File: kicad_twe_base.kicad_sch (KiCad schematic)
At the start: 5 parts

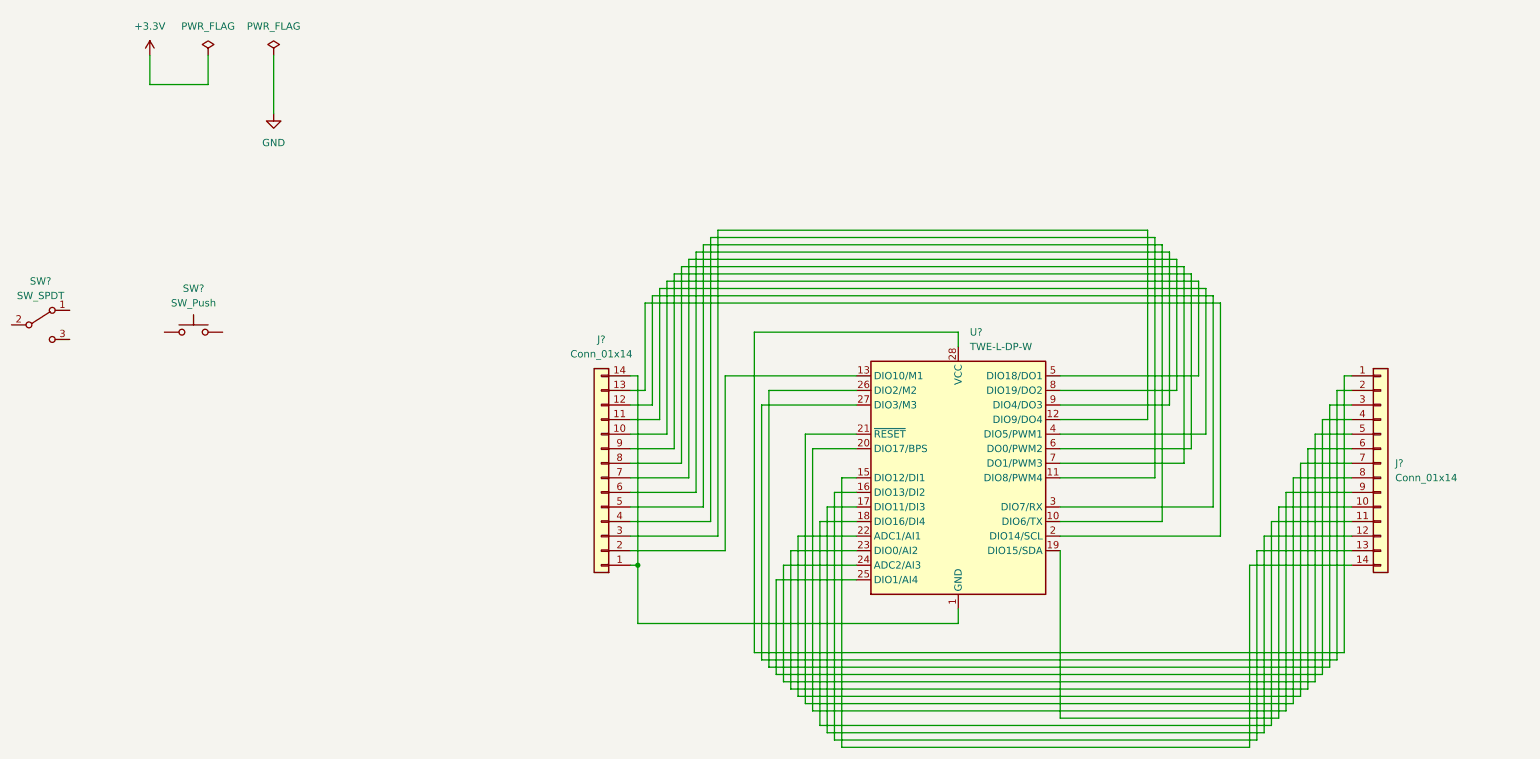
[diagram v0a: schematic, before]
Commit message: TWELITE周辺の配線を修正
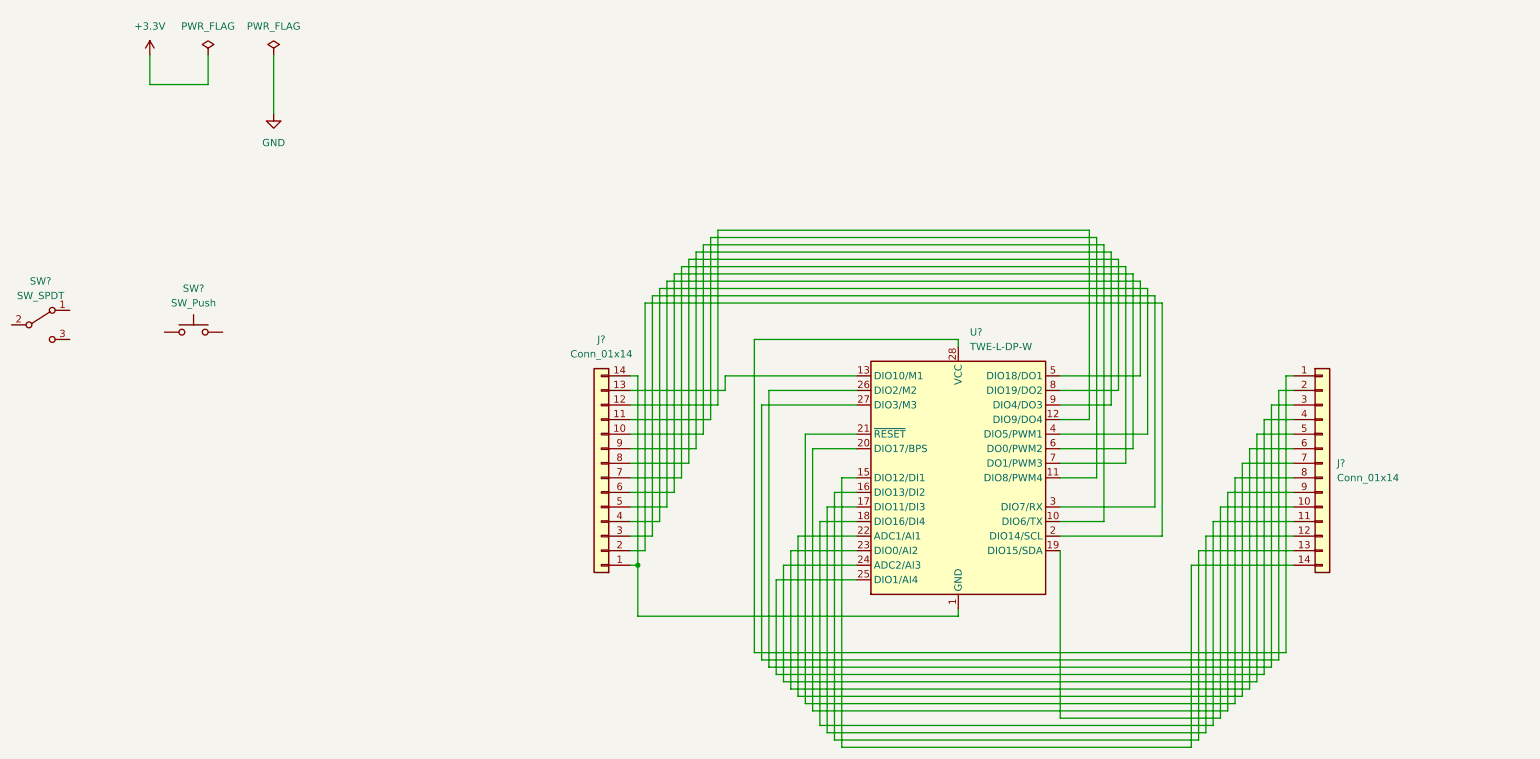
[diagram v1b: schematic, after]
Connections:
- net at U?.10 (DIO6/TX): now also J?.10 (Pin_10); no longer J?.5 (Pin_5)
- net at U?.11 (DIO8/PWM4): now also J?.11 (Pin_11); no longer J?.4 (Pin_4)
- net at U?.12 (DIO9/DO4): now also J?.12 (Pin_12); no longer J?.3 (Pin_3)
- net at U?.13 (DIO10/M1): now also J?.13 (Pin_13); no longer J?.2 (Pin_2)
- net at U?.2 (DIO14/SCL): now also J?.2 (Pin_2); no longer J?.13 (Pin_13)
- net at U?.3 (DIO7/RX): now also J?.3 (Pin_3); no longer J?.12 (Pin_12)
- net at U?.4 (DIO5/PWM1): now also J?.4 (Pin_4); no longer J?.11 (Pin_11)
- net at U?.5 (DIO18/DO1): now also J?.5 (Pin_5); no longer J?.10 (Pin_10)
- net at U?.6 (DO0/PWM2): now also J?.6 (Pin_6); no longer J?.9 (Pin_9)
- net at U?.7 (DO1/PWM3): now also J?.7 (Pin_7); no longer J?.8 (Pin_8)
- net at U?.8 (DIO19/DO2): now also J?.8 (Pin_8); no longer J?.7 (Pin_7)
- net at U?.9 (DIO4/DO3): now also J?.9 (Pin_9); no longer J?.6 (Pin_6)
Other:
- moved on the sheet: J?

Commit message: TWELITE R2用の書き込み端子を用意した
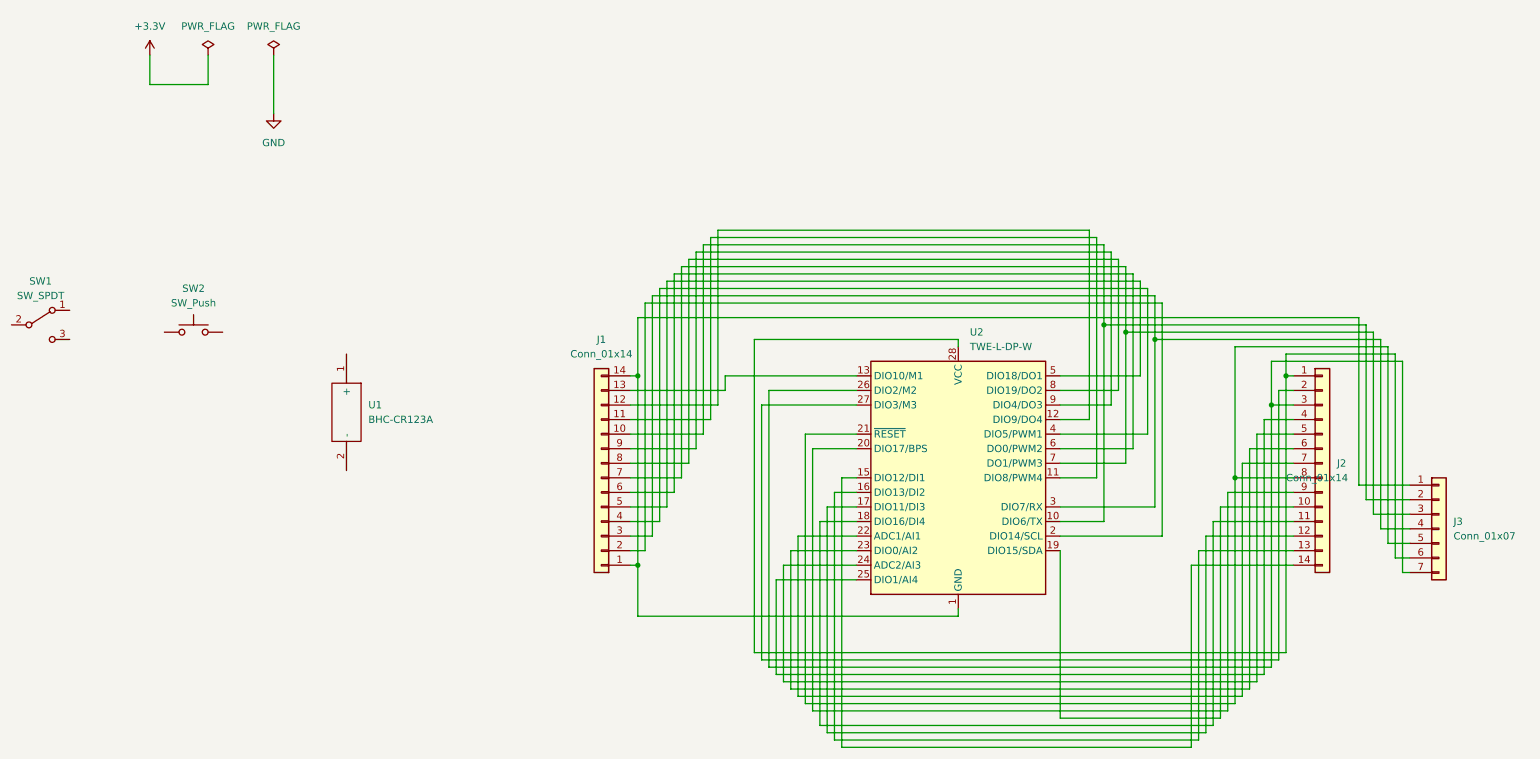
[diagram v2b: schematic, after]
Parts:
- added J3: Conn_01x07, Connector_PinHeader_2.54mm:PinHeader_1x07_P2.54mm_Vertical, symbol Connector_Generic:Conn_01x07
- added U1: BHC-CR123A, BHC-CR123A, symbol BHC-CR123A:BHC-CR123A
- J1, J2: renamed from J?; footprint (none) -> Connector_PinHeader_2.54mm:PinHeader_1x14_P2.54mm_Vertical
- gave numbers to parts that had none: 3
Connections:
- net at J1.1 (Pin_1), J1.14 (Pin_14), U2.1 (GND)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: now also J3.1 (Pin_1)
- net at J1.10 (Pin_10), U2.10 (DIO6/TX): now also J3.2 (Pin_2)
- net at J2.8 (Pin_8), U2.21 (~{RESET}): now also J3.5 (Pin_5)
- net at J2.3 (Pin_3), U2.26 (DIO2/M2): now also J3.7 (Pin_7)
- net at J2.1 (Pin_1), U2.28 (VCC): now also J3.6 (Pin_6)
- net at J1.3 (Pin_3), U2.3 (DIO7/RX): now also J3.4 (Pin_4)
- net at J1.7 (Pin_7), U2.7 (DO1/PWM3): now also J3.3 (Pin_3)

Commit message: 配線完了 ERC NG
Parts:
- added JP1: SolderJumper_3_Open, symbol Jumper:SolderJumper_3_Open
- added SW3: SW_SPDT, symbol Switch:SW_SPDT
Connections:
- net GND: now also J1.1 (Pin_1), J1.14 (Pin_14), J3.1 (Pin_1), SW1.3 (C), SW2.2, U1.2 (-), U2.1 (GND), U2.14 (GND)
- net at SW1.2 (B): now also J2.3 (Pin_3), J3.7 (Pin_7), U2.26 (DIO2/M2)
- net at J2.8 (Pin_8), J3.5 (Pin_5), U2.21 (~{RESET}): now also SW2.1
- net at J2.1 (Pin_1), U2.28 (VCC): now also JP1.2 (C), SW3.2 (B); no longer J3.6 (Pin_6)
- net at U1.1 (+): now also JP1.3 (B), SW3.1 (A)
- new net: J3.6 (Pin_6), JP1.1 (A), SW3.3 (C)
- no-connect marks 0 -> 1
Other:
- moved on the sheet: SW1, SW2, U1

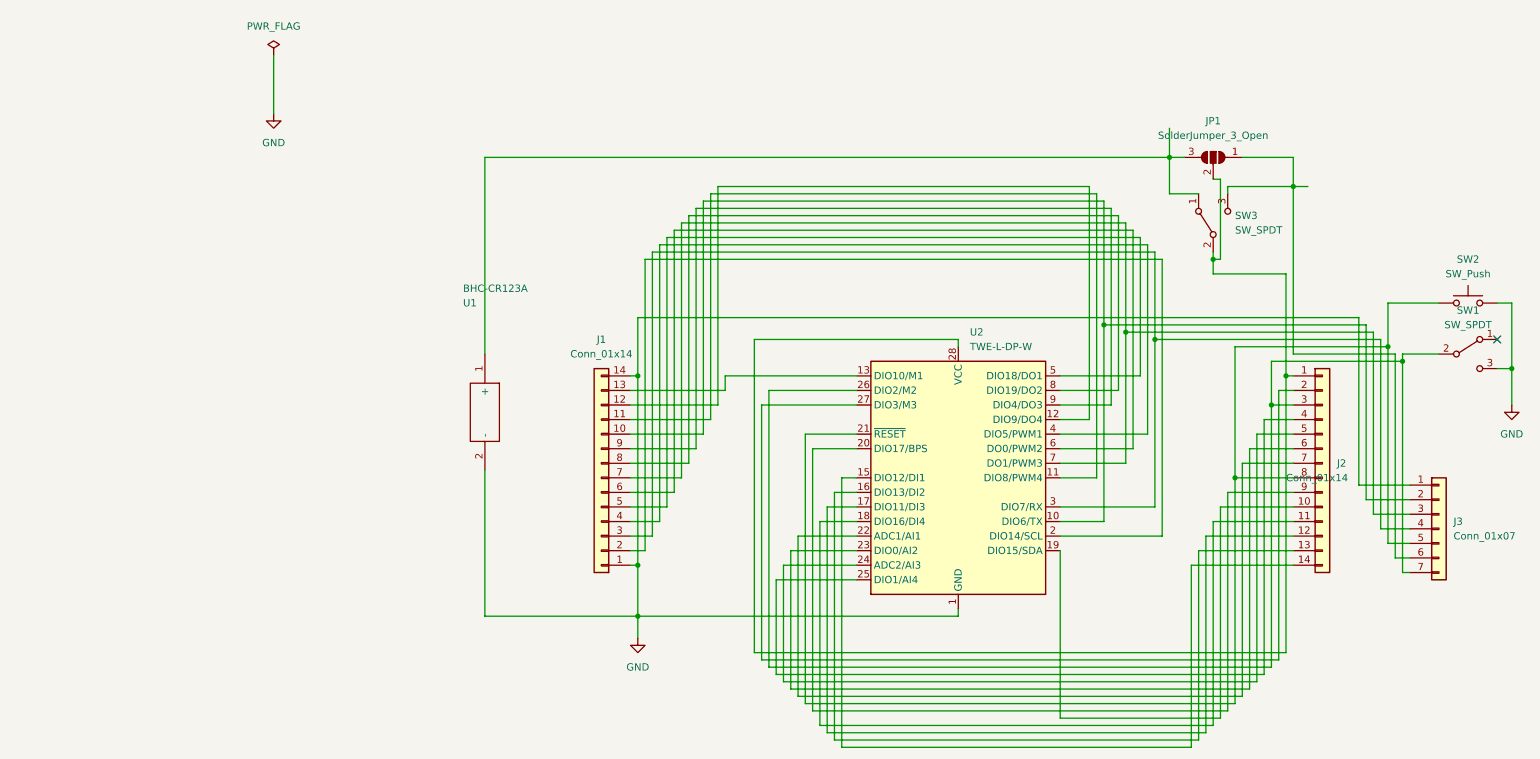
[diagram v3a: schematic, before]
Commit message: 3v3,GNDのPWR_FLGを削除
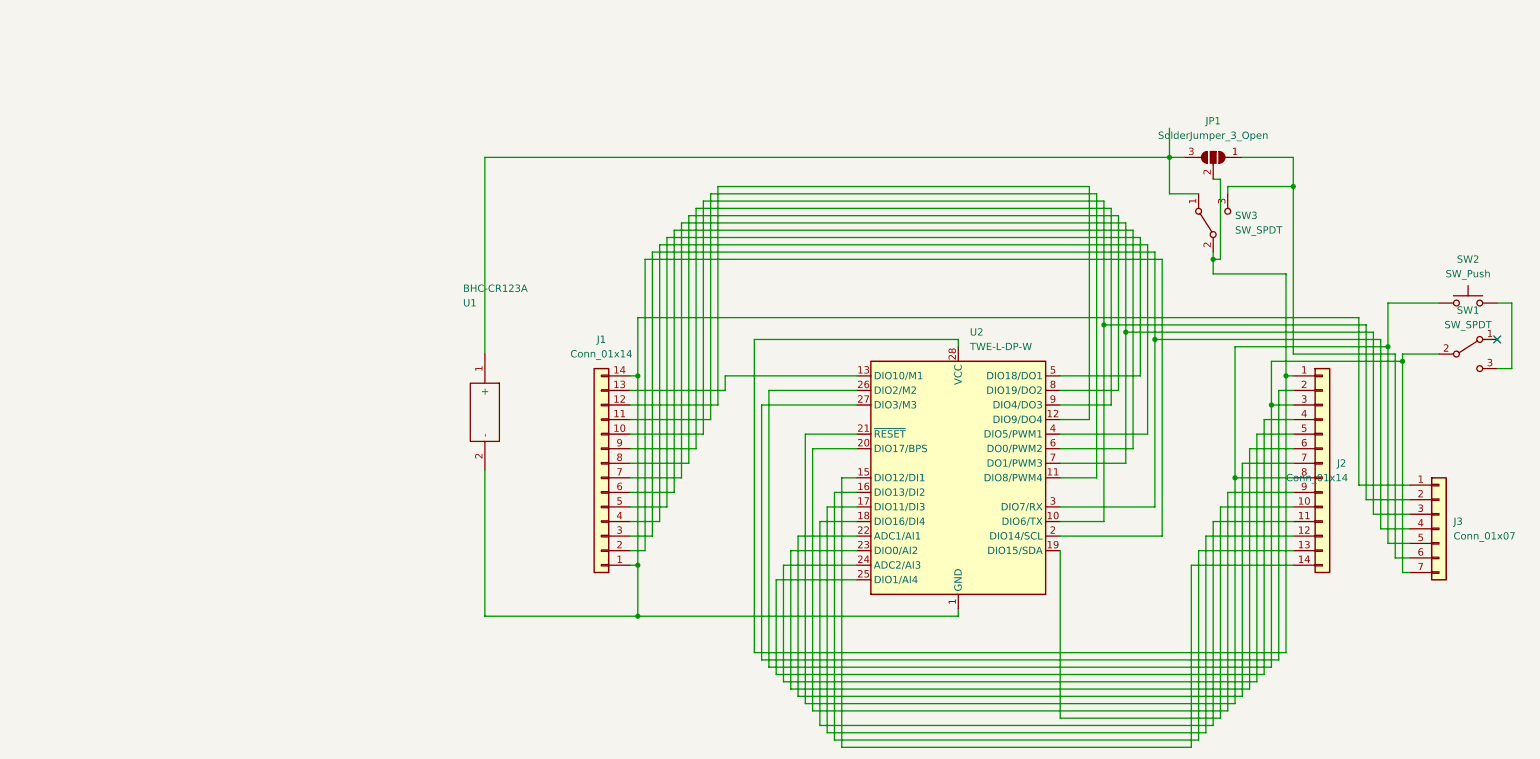
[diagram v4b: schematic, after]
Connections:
- net GND: no longer names the net of J1.1 (Pin_1), J1.14 (Pin_14), J3.1 (Pin_1), U1.2 (-), U2.1 (GND), U2.14 (GND)
- net GND: no longer SW1.3 (C), SW2.2
- new net: SW1.3 (C), SW2.2
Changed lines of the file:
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@@
 (kicad_sch (version 20211123) (generator eeschema)
   (paper "A4")
-  (junction (at 255.27 73.66) (diameter 0) (color 0 0 0 0)
-  )
   (junction (at 102.87 74.93) (diameter 0) (color 0 0 0 0)
   )
@@
     (stroke (width 0) (type default) (color 0 0 0 0))
   )
-  (wire (pts (xy 102.87 116.84) (xy 102.87 120.65))
-    (stroke (width 0) (type default) (color 0 0 0 0))
-  )
   (wire (pts (xy 208.28 90.17) (xy 208.28 130.81))
     (stroke (width 0) (type default) (color 0 0 0 0))
@@
     (stroke (width 0) (type default) (color 0 0 0 0))
   )
-  (wire (pts (xy 39.37 19.05) (xy 39.37 29.21))
-    (stroke (width 0) (type default) (color 0 0 0 0))
-  )
   (wire (pts (xy 213.36 80.01) (xy 213.36 125.73))
     (stroke (width 0) (type default) (color 0 0 0 0))
@@
     (stroke (width 0) (type default) (color 0 0 0 0))
   )
-  (wire (pts (xy 255.27 73.66) (xy 255.27 80.01))
-    (stroke (width 0) (type default) (color 0 0 0 0))
-  )
   (wire (pts (xy 127 127) (xy 127 110.49))
     (stroke (width 0) (type default) (color 0 0 0 0))
@@
   )
   (wire (pts (xy 114.3 85.09) (xy 114.3 44.45))
-    (stroke (width 0) (type default) (color 0 0 0 0))
-  )
-  (wire (pts (xy 217.17 41.91) (xy 219.71 41.91))
     (stroke (width 0) (type default) (color 0 0 0 0))
   )
@@
     (pin "7")
   )
-  (symbol (lib_id "power:GND") (at 39.37 29.21 0) (unit 1)
-    (in_bom yes) (on_board yes) (fields_autoplaced)
-    (property "Reference" "#PWR0102" (id 0) (at 39.37 35.56 0)
-      (effects (font (size 1.27 1.27)) hide)
-    )
-    (property "Value" "GND" (id 1) (at 39.37 34.29 0))
-    (property "Footprint" "" (id 2) (at 39.37 29.21 0)
-      (effects (font (size 1.27 1.27)) hide)
-    )
-    (property "Datasheet" "" (id 3) (at 39.37 29.21 0)
-      (effects (font (size 1.27 1.27)) hide)
-    )
-    (pin "1")
-  )
   (symbol (lib_id "BHC-CR123A:BHC-CR123A") (at 76.2 71.12 270) (unit 1)
     (in_bom yes) (on_board yes) (fields_autoplaced)
@@
     (pin "1")
     (pin "2")
-  )
-  (symbol (lib_id "power:PWR_FLAG") (at 39.37 19.05 0) (unit 1)
-    (in_bom yes) (on_board yes) (fields_autoplaced)
-    (property "Reference" "#FLG0102" (id 0) (at 39.37 17.145 0)
-      (effects (font (size 1.27 1.27)) hide)
-    )
-    (property "Value" "PWR_FLAG" (id 1) (at 39.37 13.97 0))
-    (property "Footprint" "" (id 2) (at 39.37 19.05 0)
-      (effects (font (size 1.27 1.27)) hide)
-    )
-    (property "Datasheet" "~" (id 3) (at 39.37 19.05 0)
-      (effects (font (size 1.27 1.27)) hide)
-    )
-    (pin "1")
   )
   (symbol (lib_id "Switch:SW_Push") (at 247.65 62.23 0) (unit 1)
@@
     (pin "2")
   )
-  (symbol (lib_id "power:GND") (at 255.27 80.01 0) (unit 1)
-    (in_bom yes) (on_board yes) (fields_autoplaced)
-    (property "Reference" "#PWR0103" (id 0) (at 255.27 86.36 0)
-      (effects (font (size 1.27 1.27)) hide)
-    )
-    (property "Value" "GND" (id 1) (at 255.27 85.09 0))
-    (property "Footprint" "" (id 2) (at 255.27 80.01 0)
-      (effects (font (size 1.27 1.27)) hide)
-    )
-    (property "Datasheet" "" (id 3) (at 255.27 80.01 0)
-      (effects (font (size 1.27 1.27)) hide)
-    )
-    (pin "1")
-  )
-  (symbol (lib_id "power:GND") (at 102.87 120.65 0) (unit 1)
-    (in_bom yes) (on_board yes) (fields_autoplaced)
-    (property "Reference" "#PWR0101" (id 0) (at 102.87 127 0)
-      (effects (font (size 1.27 1.27)) hide)
-    )
-    (property "Value" "GND" (id 1) (at 102.87 125.73 0))
-    (property "Footprint" "" (id 2) (at 102.87 120.65 0)
-      (effects (font (size 1.27 1.27)) hide)
-    )
-    (property "Datasheet" "" (id 3) (at 102.87 120.65 0)
-      (effects (font (size 1.27 1.27)) hide)
-    )
-    (pin "1")
-  )
   (sheet_instances
     (path "/" (page "1"))
   )
   (symbol_instances
-    (path "/a495c44c-0621-4b81-8568-15d3eeb6bd10"
-      (reference "#FLG0102") (unit 1) (value "PWR_FLAG") (footprint "")
-    )
-    (path "/e732eca9-81ef-4a3c-8c78-3c7e5283bbfe"
-      (reference "#PWR0101") (unit 1) (value "GND") (footprint "")
-    )
-    (path "/8142001c-a9d5-457a-9968-95120d035d39"
-      (reference "#PWR0102") (unit 1) (value "GND") (footprint "")
-    )
-    (path "/e48c1c50-151e-43db-867d-ea2cac1dc8ea"
-      (reference "#PWR0103") (unit 1) (value "GND") (footprint "")
-    )
     (path "/582347dd-481e-41b1-b01e-de3b4055c2be"
       (reference "J1") (unit 1) (value "Conn_01x14") (footprint "Connector_PinHeader_2.54mm:PinHeader_1x14_P2.54mm_Vertical")
